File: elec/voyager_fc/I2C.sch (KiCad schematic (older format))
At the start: 39 parts

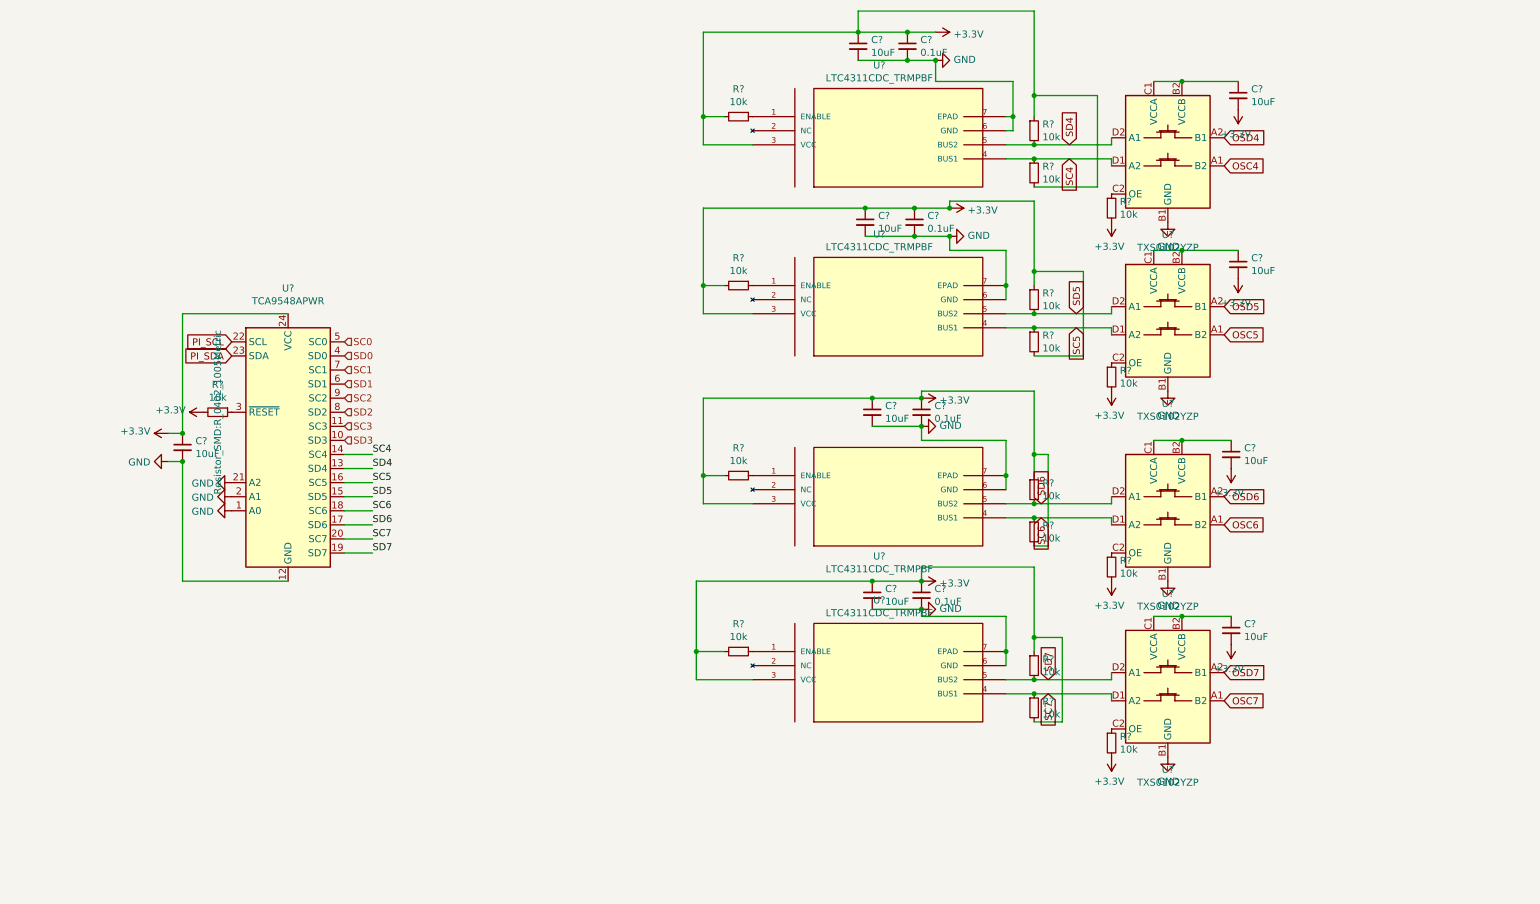
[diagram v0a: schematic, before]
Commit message: Move connectors inside schematics
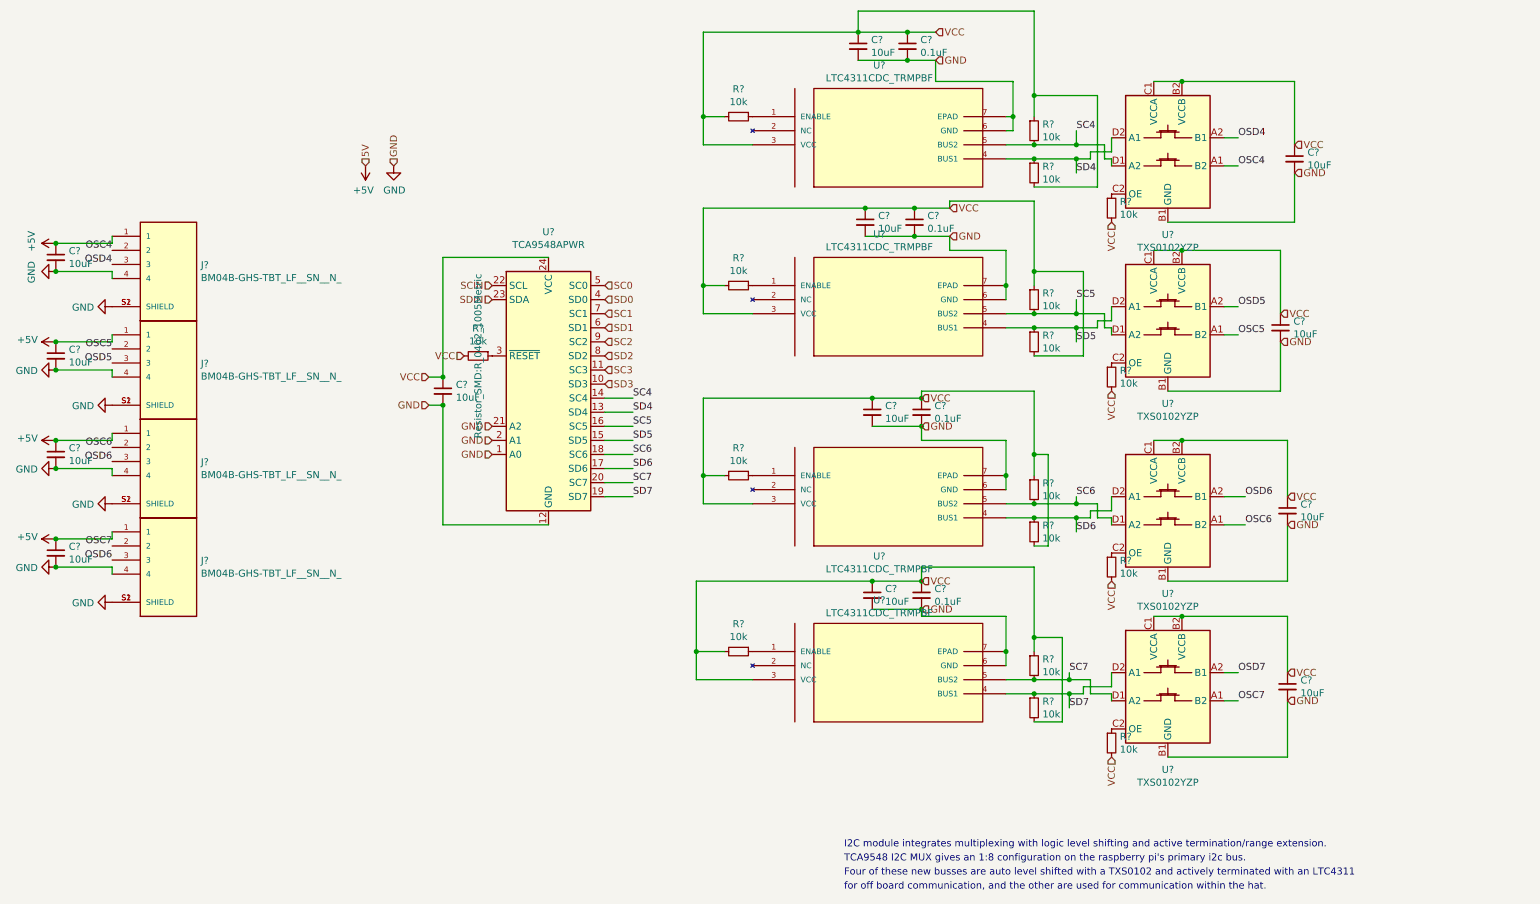
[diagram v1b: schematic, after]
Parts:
- removed C? (x3): 10uF, Capacitor_SMD:C_0504_1310Metric, symbol Device:C_Small
- added C? (x7): 10uF, Capacitor_SMD:C_0504_1310Metric, symbol Device:C_Small
- added J? (x4): BM04B-GHS-TBT_LF__SN__N_, JST_BM04B-GHS-TBT_LF__SN__N_, symbol BM04B-GHS-TBT_LF__SN__N_:BM04B-GHS-TBT_LF__SN__N_
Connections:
- net GND: now also C?.2, C?.2, C?.2, C?.2, C?.2, C?.2, C?.2, C?.2, J?.4, J?.4, J?.4, J?.4, J?.S1 (SHIELD), J?.S1 (SHIELD), J?.S1 (SHIELD), J?.S1 (SHIELD), J?.S2 (SHIELD), J?.S2 (SHIELD), J?.S2 (SHIELD), J?.S2 (SHIELD)
- net OSC4: now also J?.2
- net OSC5: now also J?.2
- net OSC6: now also J?.2
- net OSC7: now also J?.2
- net OSD4: now also J?.3
- net OSD5: now also J?.3
- net OSD6: now also J?.3, J?.3
- net SC4: now also R?.2, U?.5 (BUS2); no longer R?.1, U?.4 (BUS1)
- net SC5: now also R?.2, U?.5 (BUS2); no longer R?.1, U?.4 (BUS1)
- net SC6: now also R?.2, U?.5 (BUS2); no longer R?.1, U?.4 (BUS1)
- net SC7: now also R?.2, U?.5 (BUS2); no longer R?.1, U?.4 (BUS1)
- net SD4: now also R?.1, U?.4 (BUS1); no longer R?.2, U?.5 (BUS2)
- net SD5: now also R?.1, U?.4 (BUS1); no longer R?.2, U?.5 (BUS2)
- net SD6: now also R?.1, U?.4 (BUS1); no longer R?.2, U?.5 (BUS2)
- net SD7: now also R?.1, U?.4 (BUS1); no longer R?.2, U?.5 (BUS2)
- net VCC: now reaches C?.1, U?.B2 (VCCB), U?.C1 (VCCA)
- net VCC: now also C?.1, C?.1, C?.1, C?.1, C?.1, C?.1, C?.1, C?.1, C?.1, R?.1, R?.1, R?.1, R?.1, R?.2, R?.2, R?.2, R?.2, R?.2, R?.2, R?.2, R?.2, R?.2, R?.2, R?.2, R?.2, R?.2, U?.24 (VCC), U?.3 (VCC), U?.3 (VCC), U?.3 (VCC), U?.3 (VCC), U?.B2 (VCCB), U?.B2 (VCCB), U?.B2 (VCCB), U?.C1 (VCCA), U?.C1 (VCCA), U?.C1 (VCCA), C?.1, C?.1, C?.1
- removed net +3V3: C?.1, C?.1, C?.1, C?.1, C?.1, C?.1, C?.1, C?.1, C?.1, C?.2, R?.1, R?.1, R?.1, R?.1, R?.2, R?.2, R?.2, R?.2, R?.2, R?.2, R?.2, R?.2, R?.2, R?.2, R?.2, R?.2, R?.2, U?.24 (VCC), U?.3 (VCC), U?.3 (VCC), U?.3 (VCC), U?.3 (VCC)
- net PI_SCL renamed SCIN
- net PI_SDA renamed SDIN
- new net +5V: C?.1, C?.1, C?.1, C?.1, J?.1, J?.1, J?.1, J?.1
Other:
- note added: "Four of these new busses are auto level shifted with a TXS0102 and actively terminated with an LTC4311"
- note added: "I2C module integrates multiplexing with logic level shifting and active termination/range extension."
- note added: "TCA9548 I2C MUX gives an 1:8 configuration on the raspberry pi's primary i2c bus."
- note added: "for off board communication, and the other are used for communication within the hat."
- moved on the sheet: C?, R?, U?

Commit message: Place all components and start route
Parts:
- C40, C41, C42, C43, C45, C46, C47, C48, C53, C54, C55, C56: renamed from C?; footprint Capacitor_SMD:C_0504_1310Metric -> Capacitor_SMD:C_0603_1608Metric
- C44: renamed from C?; footprint Capacitor_SMD:C_0805_2012Metric -> Capacitor_SMD:C_0603_1608Metric
- C49, C50, C51, C52: renamed from C?; footprint Capacitor_SMD:C_0504_1310Metric -> Capacitor_SMD:C_0402_1005Metric
- J21, J22, J23, J24: renamed from J?; footprint JST_BM04B-GHS-TBT_LF__SN__N_ -> BM04B-GHS-TBT_LF__SN__N_:JST_BM04B-GHS-TBT_LF__SN__N_
- R58, R59, R60, R61, R62, R63, R64, R65, R66, R67, R68, R69, R70, R71, R72, R73, R74: renamed from R?; footprint Resistor_SMD:R_0402_1005Metric -> Resistor_SMD:R_0603_1608Metric
- U11, U12, U13, U14: renamed from U?; footprint DFN-6_DC -> footprint:DFN-6_DC
- gave numbers to parts that had none: 5
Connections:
- net OSD6: no longer J24.3
- net OSD7: now also J24.3
